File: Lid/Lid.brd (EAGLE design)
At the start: 111.3 x 83.7 mm, 13 parts

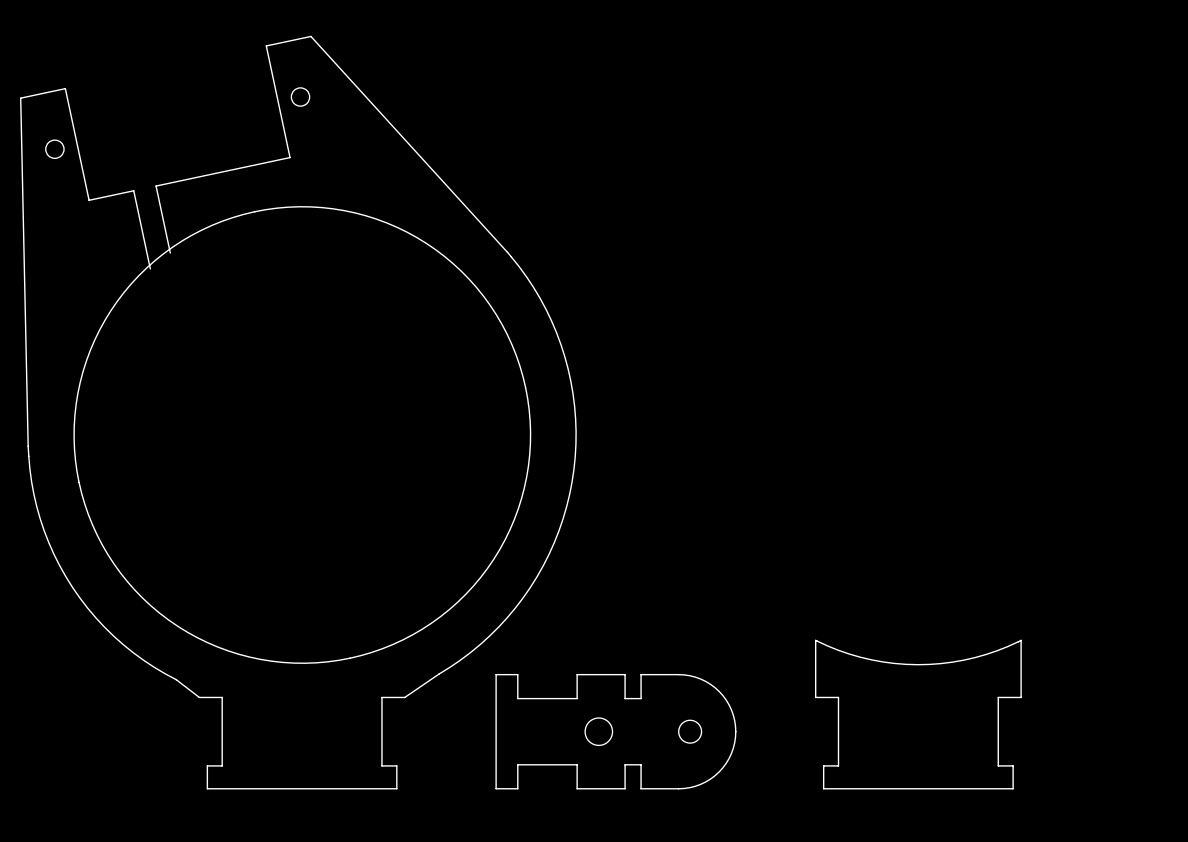
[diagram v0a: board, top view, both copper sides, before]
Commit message: widened hole and moved to 1/4" for everything (except top lid)
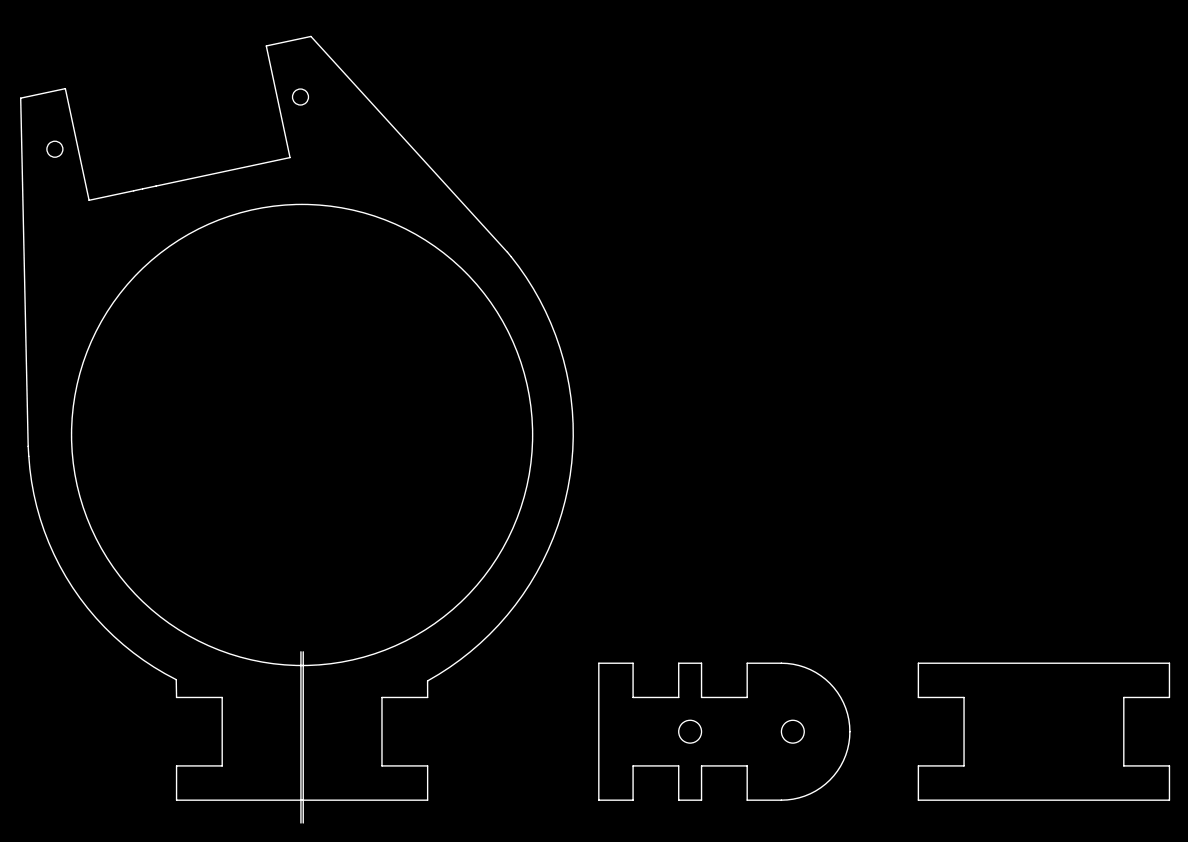
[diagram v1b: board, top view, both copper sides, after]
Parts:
- removed E$10, E$11, E$12, E$4, E$5, E$9: (no value), lid:LID_THICKNESS_060
- moved E$6 14.0 mm to (82.6, -0.00)
- moved E$3 11.4 mm to (54.6, -33.0)
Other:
- board size 111.3 x 83.7 mm -> 127.8 x 87.5 mm

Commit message: removing old dxf files
also scooted reference line out to show middle bracer is aligned, and removed second lid dia package cause it's no longer needed.
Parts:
- removed E$6: (no value), lid:CAN_DIA
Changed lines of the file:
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@@
 <wire x1="91.44" y1="-29.21" x2="91.44" y2="-36.83" width="0.1524" layer="20"/>
 <wire x1="91.44" y1="-36.83" x2="96.52" y2="-36.83" width="0.1524" layer="20"/>
-<wire x1="-35.56" y1="-25.4" x2="58.42" y2="-25.4" width="0.1524" layer="49" style="shortdash"/>
+<wire x1="-35.56" y1="-25.4" x2="104.14" y2="-25.4" width="0.1524" layer="49" style="shortdash"/>
 <wire x1="58.42" y1="-33.02" x2="-35.56" y2="-33.02" width="0.1524" layer="49" style="shortdash"/>
 <dimension x1="-35.56" y1="-25.4" x2="-35.56" y2="-33.02" x3="-38.1" y3="-29.21" textsize="1.778" layer="49" unit="inch"/>
@@
 <element name="E$2" library="lid" package="MICRO_SERVO" value="" x="-13.841925" y="34.701259375" smashed="yes" rot="R12"/>
 <element name="E$3" library="lid" package="LID_THICKNESS_060" value="" x="54.61" y="-33.02" smashed="yes" rot="R90"/>
-<element name="E$6" library="lid" package="CAN_DIA" value="" x="82.576696875" y="-0.003675" smashed="yes" rot="R12"/>
 <element name="E$7" library="lid" package="LID_THICKNESS_060" value="" x="9.652" y="-33.02" smashed="yes"/>
 <element name="E$8" library="lid" package="LID_THICKNESS_060" value="" x="-9.652" y="-33.02" smashed="yes" rot="R180"/>

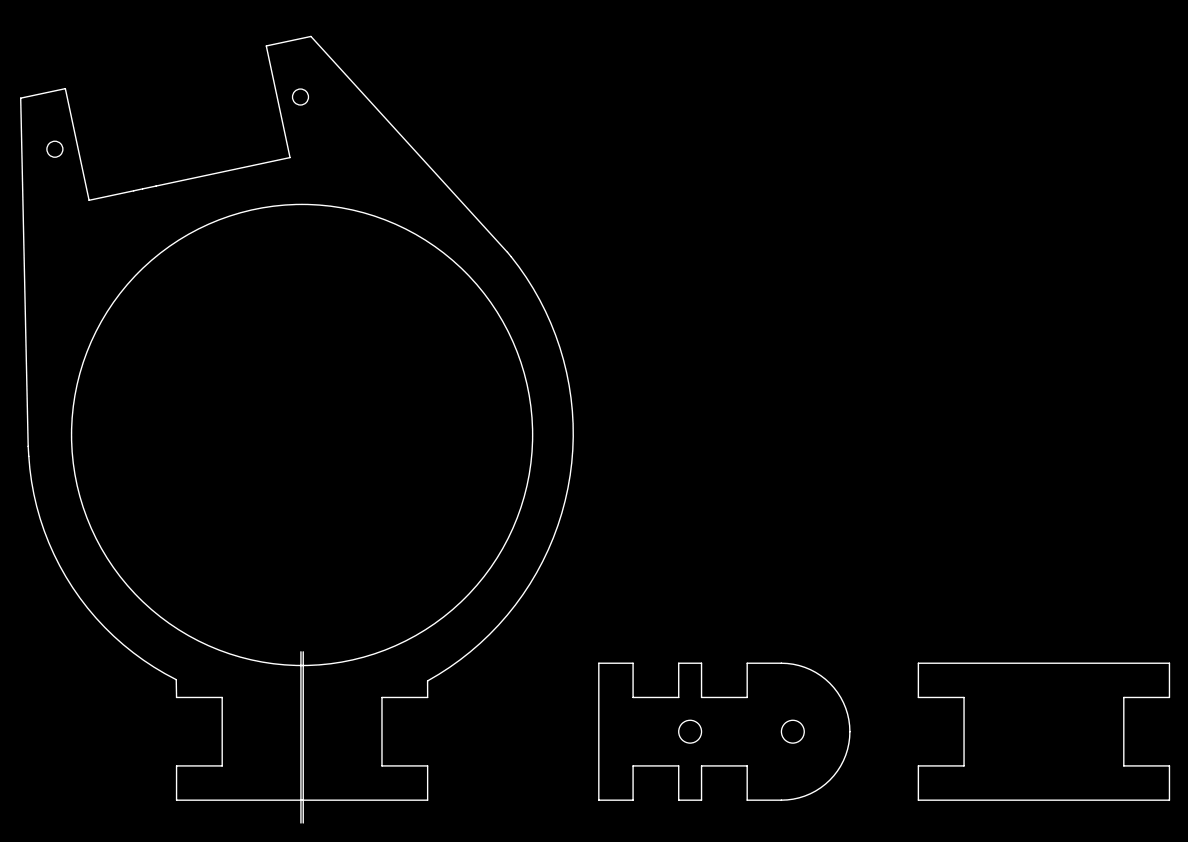
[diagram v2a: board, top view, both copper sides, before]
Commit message: Final design on lid
Tweaked the tightness on all the parts to fit snugly with the 1/4" acrylic (two prints at 10/100/5000). Also tweaked the drill hits to allow 4-40 to pass through easily and sevro screws to bite just a little.
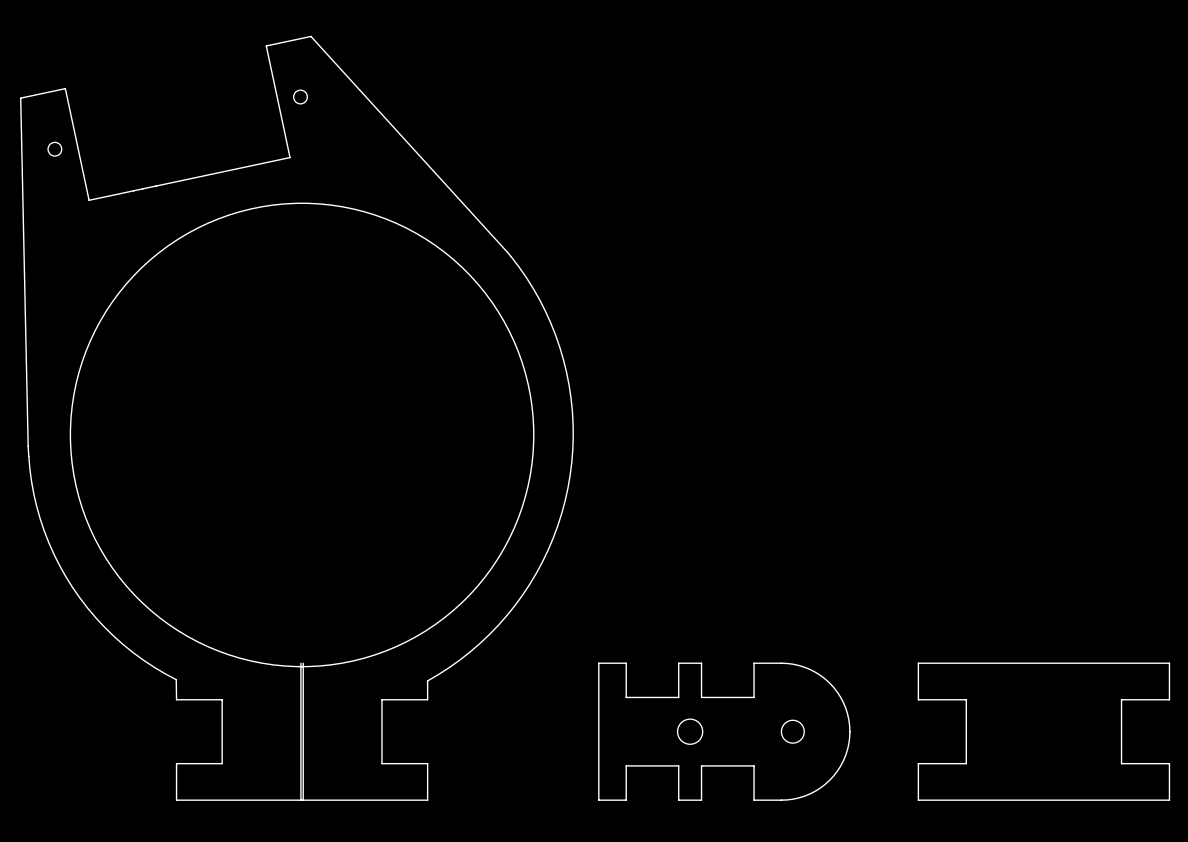
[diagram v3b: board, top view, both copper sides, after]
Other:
- board size 127.8 x 87.5 mm -> 127.8 x 85 mm

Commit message: Lid and flap done. Final versions in brd and dxf files
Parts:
- moved E$2 1.94 mm to (-14.2, 36.6)
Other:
- board size 127.8 x 85 mm -> 62.5 x 88.9 mm
- board text added: "OLD radius: 1.015 NEW: 1.018 NEWEST: 1.021"
